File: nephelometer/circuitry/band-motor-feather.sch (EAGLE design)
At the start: 63 parts, among them IC1 LM4041CILP, IC2 AD822N, IC3 MCP6S21, IC4 LP2950ACZ-3.3, J1 RJ11-6PTH, Q1 IRLB8721, T1 2N2222, T2 2N2222, T3 2N2222, T4 2N2222, T5 2N2222, T6 2N2222

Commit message: Feather motor controller board with ESD protection and up to 4 motors or 2 motors plus stepper
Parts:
- removed C10: 1µF, adafruit:C-US025-030X050
- removed C11, C14: 1.2nF, adafruit:C-US025-025X050
- removed C12, C7: 100nF, adafruit:C-US025-025X050
- removed C13: 1uF, adafruit:C-US025-025X050
- removed C8: 10µF, adafruit:CPOL-USE2.5-5
- removed C9: 22µF, adafruit:C-US050-045X075
- removed D$11: BPV10NF, ingolia:BPV10NF
- removed IC3: MCP6S21, ingolia:MCP6S21
- removed IC4: LP2950ACZ-3.3, v-reg:LP2950ACZ-3.3
- removed LD1: (no value), led:DUOLED-RG-C
- removed U$6: LED3MM_H101C, ingolia:LED3MM_H101C
- removed U$7: FEATHER_M0, ingolia:FEATHER_M0
- removed U$8: MAX144, ingolia:MAX144
- added D10, D9: 1N4935, adafruit:1N4004
- added D7, D8: (no value), diode:ZENER-DIODEF126-10
- added J10, J2, J5, J7, J8, J9: MotA, ingolia:1X02_3.5MM_MOT
- added J3, J6: AUDIO-JACK2PTH, SparkFun-Connectors:AUDIO-JACK2PTH
- added J4: RJ11-6PTH, SparkFun-Connectors:RJ11-6PTH
- added LED2, LED3, LED4, LED5: (no value), adafruit:LED3MM
- added MCU1: FEATHER_M0, ingolia:FEATHER_M0
- added Q2, Q3, Q4: (no value), ingolia:IRLB8721
- added R26: 1K5, adafruit:R-US_0207/10
- C1: value 100nF -> 220µF; device adafruit:C-US025-025X050 -> adafruit:CPOL-USE3.5-8; DIGIKEY# BC1084CT-ND -> P5166-ND; MANF Vishay BC Components -> Panasonic Electronic Components; MANF# K104K15X7RF5TL2 -> ECA-1VM221
- C2: value 3pF -> 0.33µ; device adafruit:C-US025-024X044 -> adafruit:C-US025-050X050; DIGIKEY# 445-8377-ND -> 445-5312-ND; MANF# FK18C0G1H030C -> FK14X7R1H334K
- C3: value 100n -> 22µ; device adafruit:C-US025-025X050 -> adafruit:C-US050-045X075; DIGIKEY# BC1084CT-ND -> 445-8455-ND; MANF Vishay BC Components -> TDK Corporation; MANF# K104K15X7RF5TL2 -> FK20X7R1C226M
- C4: value 1.2nF -> 0.33µ; device adafruit:C-US025-025X050 -> adafruit:C-US025-050X050; DIGIKEY# BC1026CT-ND -> 445-5312-ND; MANF Vishay BC Components -> TDK Corporation; MANF# K122J15C0GF5TL2 -> FK14X7R1H334K
- C5: value 100nF -> (none); DIGIKEY# BC1084CT-ND -> (none); MANF Vishay BC Components -> (none); MANF# K104K15X7RF5TL2 -> (none)
- C6: value 1.2nF -> (none); DIGIKEY# BC1026CT-ND -> (none); MANF Vishay BC Components -> (none); MANF# K122J15C0GF5TL2 -> (none)
- D2: value 5V -> 1N4935; device diode:ZENER-DIODEF126-10 -> adafruit:1N4004; DIGIKEY# (none) -> 1N4935FSCT-ND; MANF (none) -> Fairchild Semiconductor; MANF# (none) -> 1N4935
- D3: value 12V -> 1N4935; device diode:ZENER-DIODEF126-10 -> adafruit:1N4004; DIGIKEY# (none) -> 1N4935FSCT-ND; MANF (none) -> Fairchild Semiconductor; MANF# (none) -> 1N4935
- D4, D5, D6: value 12V -> (none)
- IC1: value LM4041CILP -> 7805TV; device texas:LM4041CILP -> linear:7805TV; DIGIKEY# 296-22173-1-ND -> LM7805CT-ND; MANF Texas Instruments -> Fairchild Semiconductor; MANF# LM4041CILPR -> LM7805CT
- IC2: value AD822N -> L293D; device analog-devices:AD822N -> st-microelectronics:L293D; DIGIKEY# AD823ANZ-ND -> (none); MANF Analog Devices Inc. -> (none); MANF# AD823ANZ -> (none)
- J1: value RJ11-6PTH -> PJ-102A; device SparkFun-Connectors:RJ11-6PTH -> ingolia:PJ-102A; DIGIKEY# AE10383-ND -> CP-102A-ND; MANF Assmann WSW Components -> CUI Inc.; MANF# A-2004-1-4-LP-N-R -> PJ-102A
- LED1: value LED -> (none); device ingolia:1X02_3.5MM_LED -> adafruit:LED5MM; DIGIKEY# 475-3002-ND -> 754-1735-ND; DIGIKEY2# 492-1502-ND -> (none); DIGIKEY3# ED2740-ND -> (none); MANF OSRAM Opto Semiconductors Inc -> Kingbright; MANF# SFH 4547 -> WP7113SGD; MANF2 Bivar Inc -> (none); MANF2# CR-174 -> (none); MANF3 On Shore Technology Inc. -> (none); MANF3# OSTTE020104 -> (none)
- Q1: value IRLB8721 -> (none); MANF Infineon Technologies -> International Rectifier
- R1: value 330R -> 1K0; DIGIKEY# CF14JT330RCT-ND -> S1KHCT-ND; MANF# CF14JT330R -> CFM12JT1K00
- R10: value 133K -> 2K2; device adafruit:R-US_0207/9 -> adafruit:R-US_0207/10; DIGIKEY# 133KXBK-ND -> S1KHCT-ND; MANF Yageo -> Stackpole Electronics Inc; MANF# MFR-25FBF52-133K -> CFM12JT1K00
- R11: value 10K -> 680R; device adafruit:R-US_0207/9 -> adafruit:R-US_0207/10; DIGIKEY# CF14JT4K70CT-ND -> S1KHCT-ND; MANF# CF14JT4K70 -> CFM12JT1K00
- R12: value 470R -> 10K; device adafruit:R-US_0207/9 -> adafruit:R-US_0207/10; DIGIKEY# CF14JT330RCT-ND -> CF14JT4K70CT-ND; MANF Stackpole Electronics Inc. -> Stackpole Electronics Inc; MANF# CF14JT330R -> CF14JT4K70
- R13: value 330R -> 33K; device adafruit:R-US_0207/9 -> adafruit:R-US_0207/10; DIGIKEY# 6.65KXBK-ND -> S1KHCT-ND; MANF Yageo -> Stackpole Electronics Inc; MANF# MFR-25FBF52-6K65 -> CFM12JT1K00
- R14: value 470R -> 2K2; device adafruit:R-US_0207/5V -> adafruit:R-US_0207/10; DIGIKEY# CF14JT150RCT-ND -> S1KHCT-ND; MANF Stackpole Electronics Inc. -> Stackpole Electronics Inc; MANF# CF14JT150R -> CFM12JT1K00
- R15: value 1k5 -> 680R; device adafruit:R-US_0207/9 -> adafruit:R-US_0207/10; DIGIKEY# CF14JT4K70CT-ND -> S1KHCT-ND; MANF# CF14JT4K70 -> CFM12JT1K00
- R16: value 1k5 -> 10K; device adafruit:R-US_0207/9 -> adafruit:R-US_0207/10
- R17: value 1K5 -> 33K; device adafruit:R-US_0207/9 -> adafruit:R-US_0207/10; DIGIKEY# CF14JT330RCT-ND -> S1KHCT-ND; MANF Stackpole Electronics Inc. -> Stackpole Electronics Inc; MANF# CF14JT330R -> CFM12JT1K00
- R18: value 33K -> 2K2; device adafruit:R-US_0207/9 -> adafruit:R-US_0207/10; DIGIKEY# CF14JT330RCT-ND -> S1KHCT-ND; MANF Stackpole Electronics Inc. -> Stackpole Electronics Inc; MANF# CF14JT330R -> CFM12JT1K00
- R19: value 1K5 -> 680R; device adafruit:R-US_0207/9 -> adafruit:R-US_0207/10; DIGIKEY# CF14JT330RCT-ND -> S1KHCT-ND; MANF Stackpole Electronics Inc. -> Stackpole Electronics Inc; MANF# CF14JT330R -> CFM12JT1K00
- R2: value 3K01 -> 33K; device adafruit:R-US_0207/9 -> adafruit:R-US_0207/10; DIGIKEY# RNF14FTD3K01CT-ND -> S1KHCT-ND; MANF Stackpole Electronics Inc. -> Stackpole Electronics Inc; MANF# RNF14FTD3K01 -> CFM12JT1K00
- R20, R22: device adafruit:R-US_0207/9 -> adafruit:R-US_0207/10; DIGIKEY# CF14JT330RCT-ND -> S1KHCT-ND; MANF Stackpole Electronics Inc. -> Stackpole Electronics Inc; MANF# CF14JT330R -> CFM12JT1K00
- R21, R23: value 1K5 -> 10K; device adafruit:R-US_0207/9 -> adafruit:R-US_0207/10; DIGIKEY# CF14JT330RCT-ND -> CF14JT4K70CT-ND; MANF Stackpole Electronics Inc. -> Stackpole Electronics Inc; MANF# CF14JT330R -> CF14JT4K70
- R24: value 33K -> 10K; device adafruit:R-US_0207/9 -> adafruit:R-US_0207/10; DIGIKEY# CF14JT330RCT-ND -> CF14JT4K70CT-ND; MANF Stackpole Electronics Inc. -> Stackpole Electronics Inc; MANF# CF14JT330R -> CF14JT4K70
- R25: value 470R -> 1K5; device adafruit:R-US_0207/9 -> adafruit:R-US_0207/10; MANF Stackpole Electronics Inc. -> Stackpole Electronics Inc
- R3: value 1K00 -> 2K2; device adafruit:R-US_0207/9 -> adafruit:R-US_0207/10; DIGIKEY# RNF14FTD1K00CT-ND -> S1KHCT-ND; MANF Stackpole Electronics Inc. -> Stackpole Electronics Inc; MANF# RNF14FTD1K00 -> CFM12JT1K00
- R4: value 1M0 -> 10K; device adafruit:R-US_0207/9 -> adafruit:R-US_0207/10; DIGIKEY# RNV14FAL1M00CT-ND -> CF14JT4K70CT-ND; MANF# RNV14FAL1M00 -> CF14JT4K70
- R5: value 8R2 -> 680R; device adafruit:R-US_0207/9 -> adafruit:R-US_0207/10; DIGIKEY# S8.2HCT-ND -> S1KHCT-ND; MANF Stackpole Electronics Inc. -> Stackpole Electronics Inc; MANF# CFM12JT8R20 -> CFM12JT1K00
- R6: value 3K3 -> 1K5; device adafruit:R-US_0207/9 -> adafruit:R-US_0207/10; DIGIKEY# CF14JT4K70CT-ND -> CF14JT330RCT-ND; MANF# CF14JT4K70 -> CF14JT330R
- R7: value 1K65 -> 1K5; device adafruit:R-US_0207/9 -> adafruit:R-US_0207/10; DIGIKEY# 1.65KXBK-ND -> CF14JT330RCT-ND; MANF Yageo -> Stackpole Electronics Inc; MANF# MFR-25FBF52-1K65 -> CF14JT330R
- R8: value 6K65 -> 10K; device adafruit:R-US_0207/9 -> adafruit:R-US_0207/10; DIGIKEY# 6.65KXBK-ND -> CF14JT4K70CT-ND; MANF Yageo -> Stackpole Electronics Inc; MANF# MFR-25FBF52-6K65 -> CF14JT4K70
- R9: value 10K -> 33K; device adafruit:R-US_0207/9 -> adafruit:R-US_0207/10; DIGIKEY# CF14JT4K70CT-ND -> S1KHCT-ND; MANF# CF14JT4K70 -> CFM12JT1K00
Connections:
- removed net +3V3: C1.2, C12.2, C13.2, C5.1, C7.2, C8.+, IC2P.V+, IC3.VDD, IC4.OUT, R1.2, U$8.REF, U$8.VDD
- removed net 1V65: C3.1, IC1.C, IC2A.IN+, IC2B.IN+, IC3.VREF, R1.1, R2.1, R7.2
- removed net BPF: C6.2, IC2B.OUT, IC3.IN+, R10.2
- removed net CS_ADC: U$7.6, U$8.SHDN
- removed net CS_PGA: IC3.!CS, U$7.5
- removed net FB: C2.1, D$11.K, IC2A.IN-, R4.1
- removed net LED_CTRL: R15.2, R16.1, U$7.A3/17
- removed net MISO: U$7.MISO/22, U$8.DOUT
- removed net MOSI: IC3.SI, U$7.MOSI/23
- removed net N$35: IC1.FB, R2.2, R3.2
- removed net SCK: IC3.SCK, U$7.SCK/24, U$8.SCLK
- removed net TIA: C2.2, IC2A.OUT, R4.2, R8.2
- removed net VDD: R18.1, R20.1, R22.1, R24.1, U$7.3V3
- removed net VEXT: D1.A, D2.C, J1.5, R12.2
- new net +12V: C1.+, C2.1, C5.1, D10.C, D2.C, D3.C, D4.C, D9.C, IC1.VI, IC2.VCC2, J1.3TIP, J10.+, J2.+, J3.SLEEVE, J5.+, J6.SLEEVE, J9.+, LED2.A, LED3.A, LED4.A, LED5.A, R1.2
- new net EN: IC2.1-2EN, IC2.3-4EN, R24.1
- new net MOT1_IN: D5.C, J4.3, R5.2
- new net MOT2_IN: D6.C, J4.4, R11.2
- new net MOT3_IN: D7.C, J4.1, R15.2
- new net MOT4_IN: D8.C, J4.6, R19.2
- new net N$12: R22.2, T6.B
- net +5V: now also C6.1, IC2.VCC1, J4.2, MCU1.VBUS, R12.2, R13.2, R16.2, R17.2, R2.2, R21.2, R23.2, R24.2, R4.2, R8.2; no longer C10.1, C9.1, IC4.IN, LED1.A, R14.1, R25.2, U$7.VBUS
- net GND: now also C1.-, C2.2, C4.2, C6.2, D7.A, D8.A, IC1.GND, IC2.GND1, IC2.GND2, IC2.GND3, IC2.GND4, J1.1RING, J4.5, LED1.C, MCU1.GND, Q1.S, Q2.S, Q3.S, Q4.S, T3.E, T4.E, T5.E, T6.E; no longer C1.1, C10.2, C11.1, C12.1, C13.1, C14.2, C7.1, C8.-, C9.2, D$11.A, D2.A, D3.A, IC1.A, IC2P.V-, IC3.GND, IC4.GND, J1.2, LD1.C, R3.1, R5.1, U$6.K, U$7.GND, U$8.GND
- net MOT1: now also Q1.G, R4.1, T1.C; no longer D3.C, J1.4, R17.2
- net MOT1_CTRL: now also MCU1.A4/18, R3.2; no longer T3.E, U$7.A4/18
- net MOT2: now also Q2.G, R8.1, T2.C; no longer D4.C, J1.3, R19.2
- net MOT2_CTRL: now also MCU1.A5/19, R10.2; no longer T4.E, U$7.A5/19
- net MOT3: now also IC2.1A, Q3.G, R12.1, R20.1, T3.C; no longer D6.C, J1.6, R21.2
- net MOT3_CTRL: now also MCU1.10, R14.2; no longer T5.E, U$7.10
- net MOT4: now also IC2.3A, Q4.G, R16.1, R22.1, T4.C; no longer D5.C, J1.1, R23.2
- net MOT4_CTRL: now also MCU1.11, R18.2; no longer T6.E, U$7.11
- net N$1: now also LED1.A, R1.1; no longer R19.1, T4.C
- net N$10: now also R10.1, R11.1, R9.1, T2.B; no longer R23.1, T6.C
- net N$11: now also IC2.4A, R23.1, T6.C; no longer R14.2, T2.C, U$6.A
- net N$13: now also IC2.2A, R21.1, T5.C; no longer R11.1, R6.1, T1.B
- net N$14: now also R20.2, T5.B; no longer Q1.S, R5.2, R6.2
- net N$15: now also IC2.1Y, J7.+; no longer C11.2, R11.2, R15.1
- net N$16: now also IC2.2Y, J7.-; no longer R16.2, T2.B
- net N$18: now also IC2.4Y, J8.-; no longer LED1.K, Q1.D
- net N$19: now also IC2.3Y, J8.+; no longer R17.1, T3.C
- net N$2: now also C3.1, C4.1, D1.A, IC1.VO; no longer R20.2, T4.B
- net N$20: now also D9.A, J9.-, Q3.D, R25.1; no longer R18.2, T3.B
- net N$21: now also LED4.C, R25.2; no longer R24.2, T6.B
- net N$22: now also D10.A, J10.-, Q4.D, R26.1; no longer LD1.AR, R12.1
- net N$23: now also LED5.C, R26.2; no longer C14.1, R13.1, U$8.CH0, U$8.CH1
- net N$3: now also D3.A, J5.-, J6.TIP, Q2.D; no longer C4.2, C6.1, R8.1
- net N$4: now also D2.A, J2.-, J3.TIP, Q1.D, R6.1; no longer IC3.VOUT, R13.2
- net N$5: now also LED2.C, R6.2; no longer R21.1, T5.C
- net N$6: now also R2.1, R3.1, R5.1, T1.B; no longer R22.2, T5.B
- net N$7: now also LED3.C, R7.2; no longer LD1.AG, R25.1
- net N$8: now also R13.1, R14.1, R15.1, T3.B; no longer Q1.G, R9.1, T1.C
- net N$9: now also R17.1, R18.1, R19.1, T4.B; no longer C4.1, IC2B.IN-, R10.1
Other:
- note removed: "Bandpass Filter 10 kHz / Butterworth"
- note removed: "IR LED controller ~60 mA constant current"
- note removed: "SPI Analog-to-Digital"
- note removed: "SPI Programmable Gain Amplifier"
- note removed: "Separate 3.3V for analog"
- note removed: "Transimpedance Amplifier 1 V / µA, fN = 194 kHz"
- note removed: "Virtual ground shunt reg 1.65V up to 5 mA"
- moved on the sheet: C2, C3, C4, C5, C6, D1, D4, D5, D6, LED1, Q1, R1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

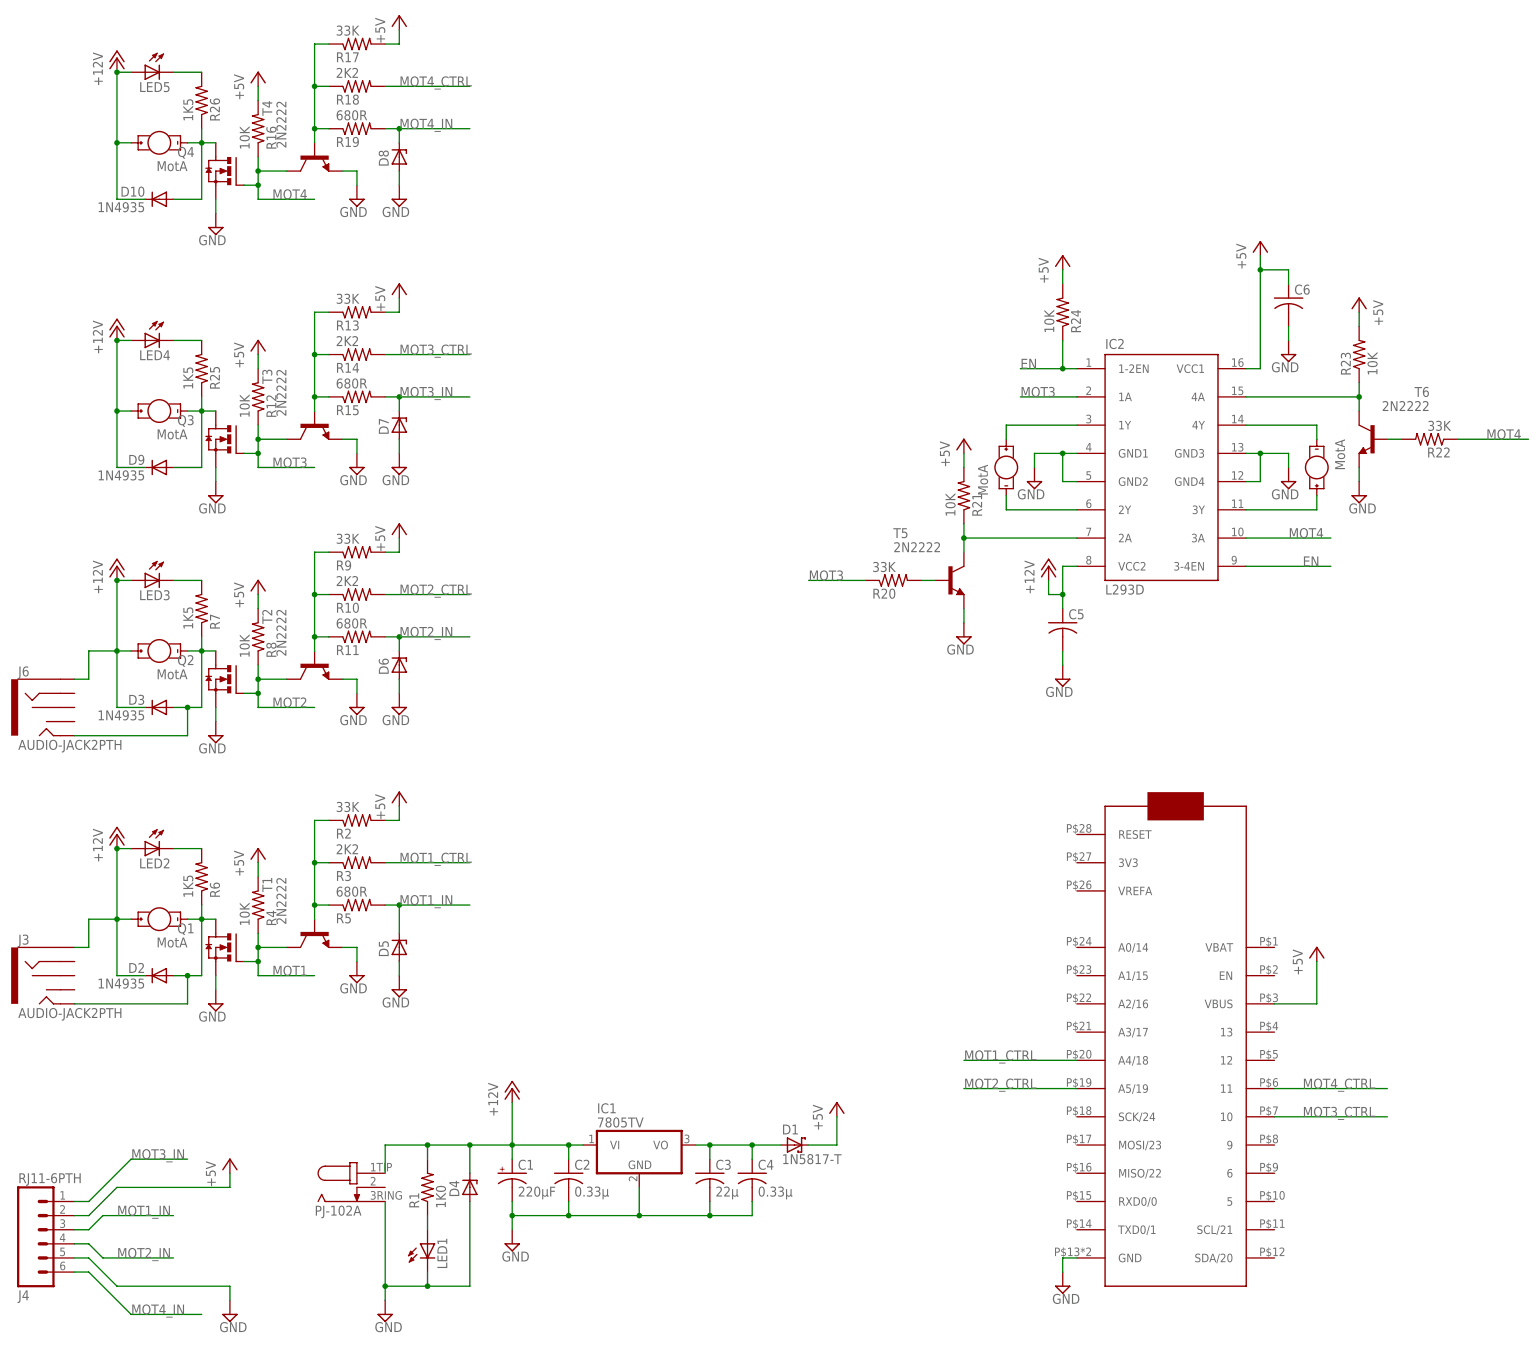
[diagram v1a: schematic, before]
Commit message: Finalized Feather nephelometer with separate ADC and 4 robust motor controls
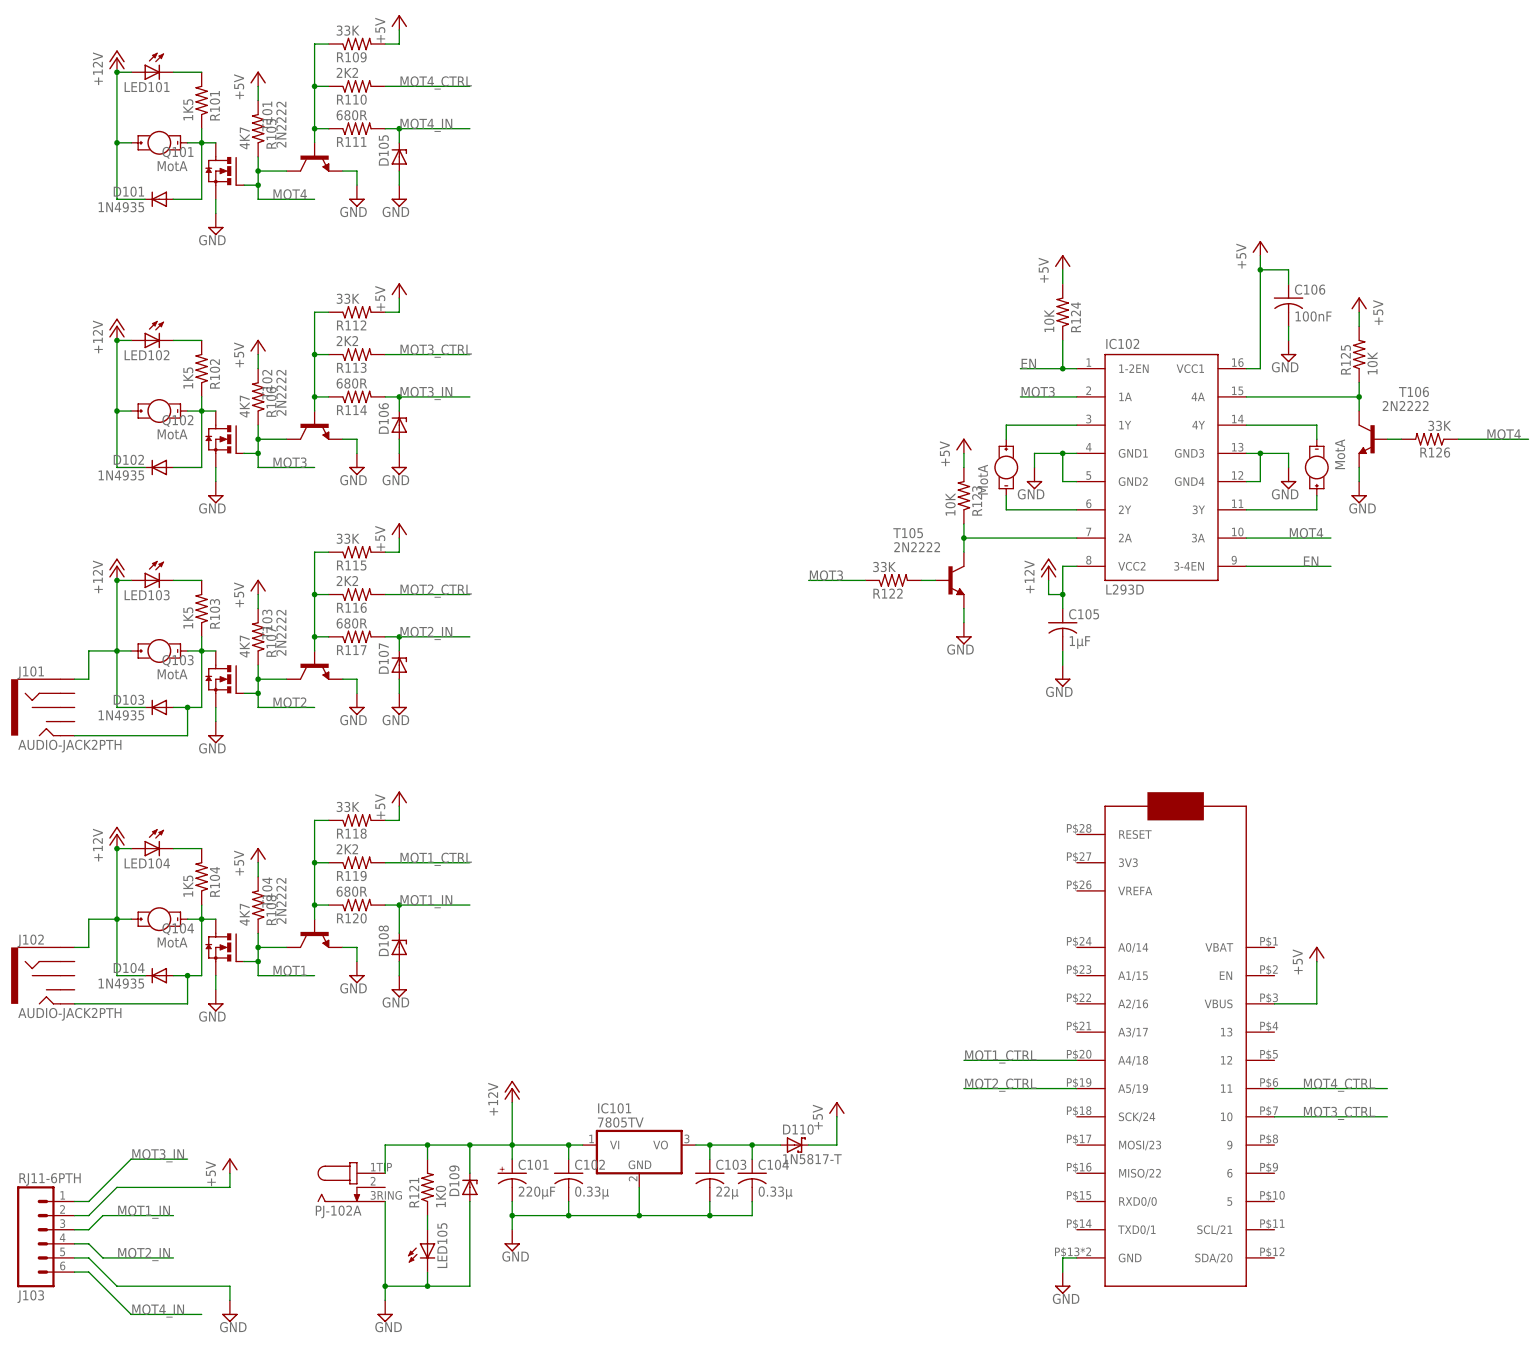
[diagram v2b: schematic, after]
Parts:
- C105: value (none) -> 1µF; DIGIKEY# (none) -> 445-5318-ND; MANF (none) -> TDK Corporation; MANF# (none) -> FK14X7R1C105K
- C106: value (none) -> 100nF; DIGIKEY# (none) -> BC1084CT-ND; MANF (none) -> Vishay BC Components; MANF# (none) -> K104K15X7RF5TL2
- D105, D106, D107, D108: DIGIKEY# (none) -> SA5.0ALFCT-ND; MANF (none) -> Littelfuse Inc.; MANF# (none) -> SA5.0A
- D109: DIGIKEY# (none) -> SA12CALFCT-ND; MANF (none) -> Littelfuse Inc.; MANF# (none) -> SA12CA
- IC102: DIGIKEY# (none) -> 296-9518-5-ND; MANF (none) -> Texas Instruments; MANF# (none) -> L293DNE
- IC103: DIGIKEY# SAM1198-14-ND -> 2830-ND; DIGIKEY2# SAM1198-14-ND -> (none); MANF Samtec Inc. -> Adafruit Industries LLC; MANF# SSQ-114-03-G-S -> 2830; MANF2 Samtec Inc. -> (none); MANF2# SSQ-114-03-G-S -> (none)
- R101, R102, R103, R104: DIGIKEY# CF14JT330RCT-ND -> CF14JT1K50CT-ND
- R105, R106, R107, R108: value 10K -> 4K7
- R109, R112, R115, R118, R122, R126: DIGIKEY# S1KHCT-ND -> CF14JT33K0CT-ND; MANF# CFM12JT1K00 -> CF14JT33K0
- R110, R113, R116, R119: DIGIKEY# S1KHCT-ND -> CF14JT2K20CT-ND; MANF# CFM12JT1K00 -> CF14JT2K20
- R111, R114, R117, R120: DIGIKEY# S1KHCT-ND -> CF14JT680RCT-ND; MANF# CFM12JT1K00 -> CF14JT680R
- R123, R124, R125: DIGIKEY# CF14JT4K70CT-ND -> CF14JT10K0CT-ND; MANF# CF14JT4K70 -> CF14JT10K0
- renumbered C1 to C101, C2 to C102, C3 to C103, C4 to C104, C5 to C105, C6 to C106, D1 to D110, D10 to D101, D2 to D104, D3 to D103, D4 to D109, D5 to D108, D6 to D107, D7 to D106, D8 to D105, D9 to D102, IC1 to IC101, IC2 to IC102, J1 to J108, J10 to J104, J2 to J107, J3 to J102, J4 to J103, J5 to J106, J6 to J101, J7 to J109, J8 to J110, J9 to J105, LED1 to LED105, LED2 to LED104, LED3 to LED103, LED4 to LED102, LED5 to LED101, MCU1 to IC103, Q1 to Q104, Q2 to Q103, Q3 to Q102, Q4 to Q101, R1 to R121, R10 to R116, R11 to R117, R12 to R106, R13 to R112, R14 to R113, R15 to R114, R16 to R105, R17 to R109, R18 to R110, R19 to R111, R2 to R118, R20 to R122, R21 to R123, R22 to R126, R23 to R125, R24 to R124, R25 to R102, R26 to R101, R3 to R119, R4 to R108, R5 to R120, R6 to R104, R7 to R103, R8 to R107, R9 to R115, T1 to T104, T2 to T103, T3 to T102, T4 to T101, T5 to T105, T6 to T106

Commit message: Minor updates after test assembly
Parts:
- D109: DIGIKEY# SA12CALFCT-ND -> SA12ALFCT-ND; MANF# SA12CA -> SA12A
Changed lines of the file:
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@@
 </part>
 <part name="D109" library="diode" deviceset="ZENER-DIODE" device="F126-10">
-<attribute name="DIGIKEY#" value="SA12CALFCT-ND"/>
+<attribute name="DIGIKEY#" value="SA12ALFCT-ND"/>
 <attribute name="MANF" value="Littelfuse Inc."/>
-<attribute name="MANF#" value="SA12CA"/>
+<attribute name="MANF#" value="SA12A"/>
 </part>
 <part name="Q103" library="ingolia" deviceset="IRLB8721" device="">
